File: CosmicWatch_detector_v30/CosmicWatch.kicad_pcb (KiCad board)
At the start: 2 copper layers, 99.9 x 99.9 mm, 81 parts, among them J3 RJ45, P1 CONN_01X04, P10 CONN_02X02, P11 CONN_01X01, P12 CONN_01X01, P13 CONN_01X01, P14 CONN_01X01, P15 CONN_02X04, P16 CONN_01X02, P19 CONN_01X01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

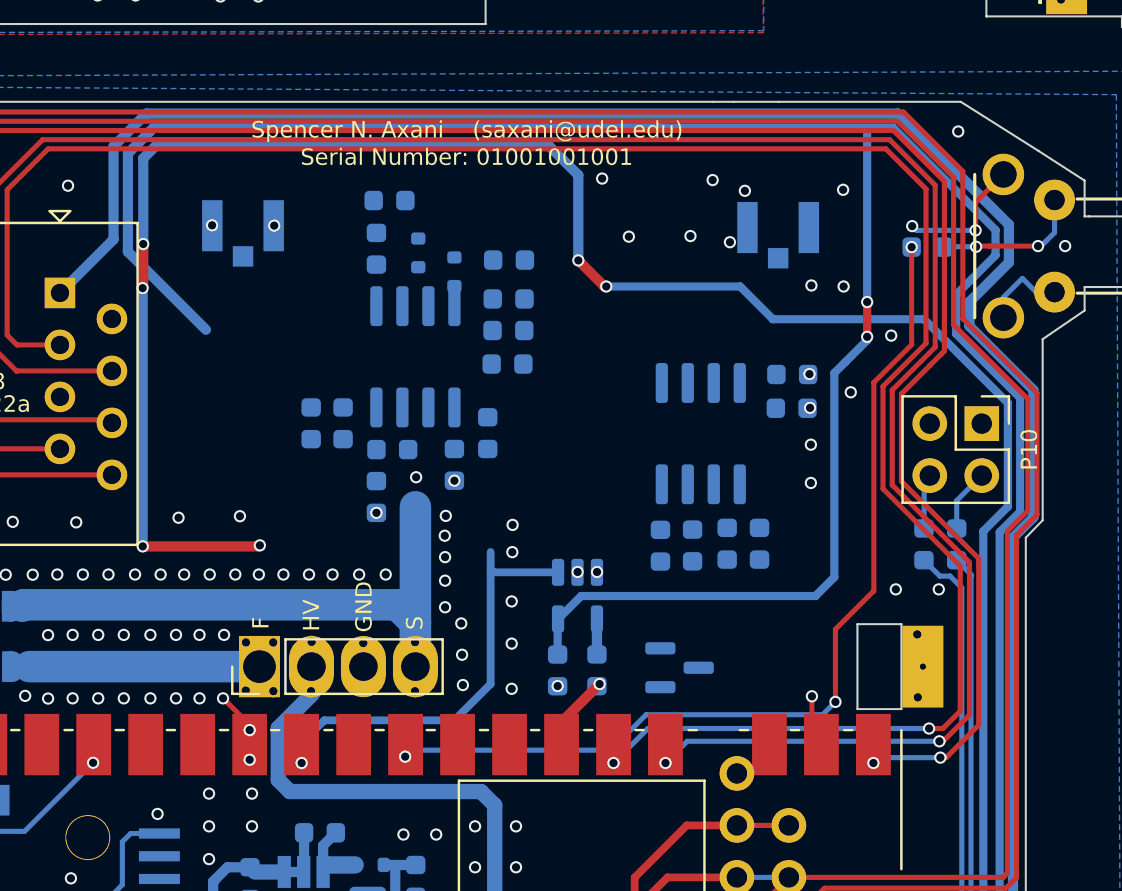
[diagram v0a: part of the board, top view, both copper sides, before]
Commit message: finished peak detector placin and wiring, starting error corrections
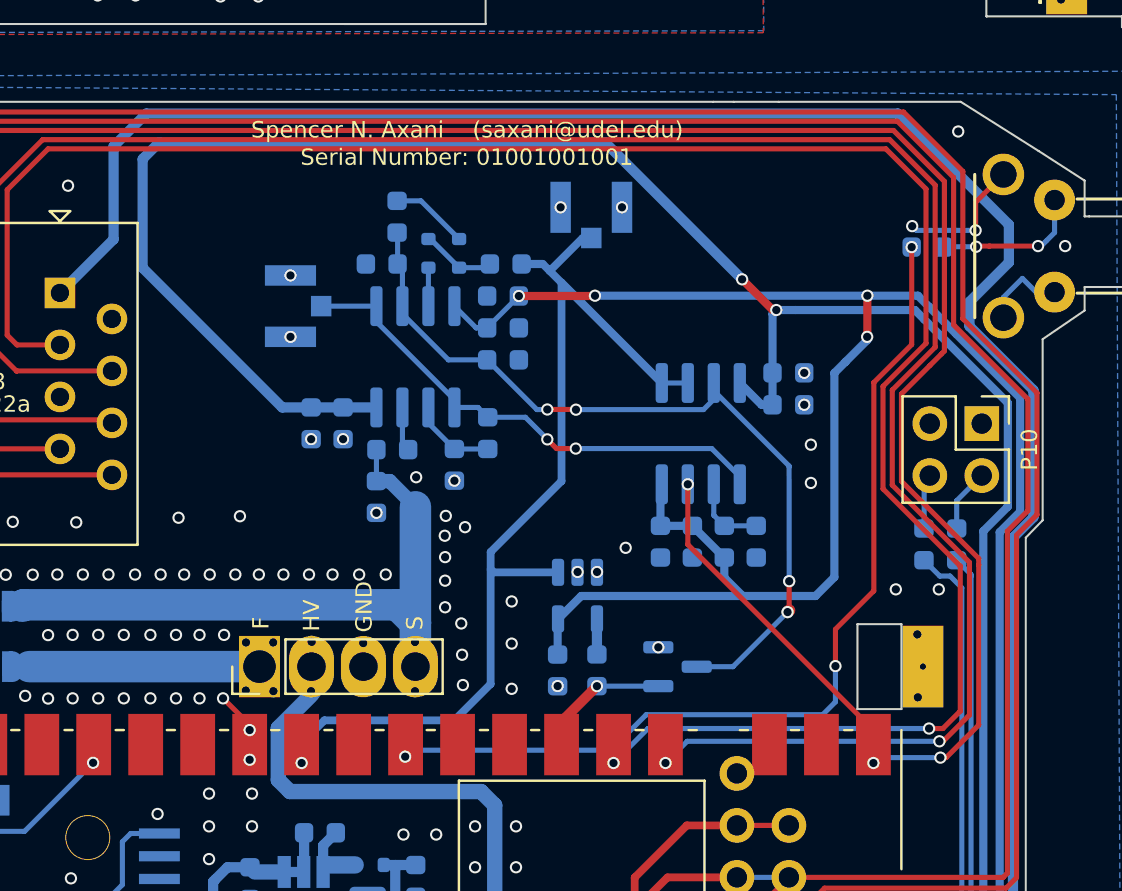
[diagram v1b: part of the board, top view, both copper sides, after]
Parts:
- moved U17 9.18 mm to (176.0, 79.7)
- moved U16 4.56 mm to (161.3, 84.5), turned to 90 degrees
- moved D3 0.93 mm to (169.6, 81.9)
- moved R9 0.87 mm to (166.5, 80.1), turned to 90 degrees
- moved C11 0.79 mm to (165.8, 82.4), turned to 0 degrees
- moved D2 0.50 mm to (168.1, 81.9)
- moved C10 0.31 mm to (171.7, 84.0)
- moved R12 0.30 mm to (171.7, 87.1)
- moved C9 0.29 mm to (171.7, 85.6)
- moved R11 0.25 mm to (171.8, 82.4)
- moved C13 0.23 mm to (185.7, 89.3)
- moved C12 0.21 mm to (185.7, 87.8)
- moved C19 0.20 mm to (179.4, 96.0)
- moved R14 0.19 mm to (184.1, 96.0)
- moved C18 0.19 mm to (181.0, 96.0)
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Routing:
- net Net-(Q1-D): track 0.00 -> 40.7 mm, vias 0 -> 4
- net VCC: track 214.6 -> 179.8 mm, vias 4 -> 6
- net SNG1: track 21.2 -> 49.1 mm, vias 2 -> 1
- net AMP1: track 0.00 -> 24.9 mm, vias 0 -> 2
- net TRG: track 110.4 -> 127.8 mm, vias 2 -> 3
- net Net-(U6--INA): track 0.00 -> 4.19 mm
- net SiPM: track 27.9 -> 31.9 mm
- net Net-(U9--INB): track 0.00 -> 3.80 mm
- net Net-(D3-K): track 0.00 -> 3.80 mm
- net Net-(D2-K): track 0.00 -> 3.66 mm
- net TriggerReset1: track 4.80 -> 7.65 mm
- net TriggerReset2: track 2.80 -> 0.00 mm, vias 1 -> 0
- net Net-(U6-+INA): track 0.00 -> 2.18 mm
- net Net-(D2-A): track 0.00 -> 1.88 mm
- net VEE: track 147.0 -> 146.2 mm, vias 6 -> 2
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
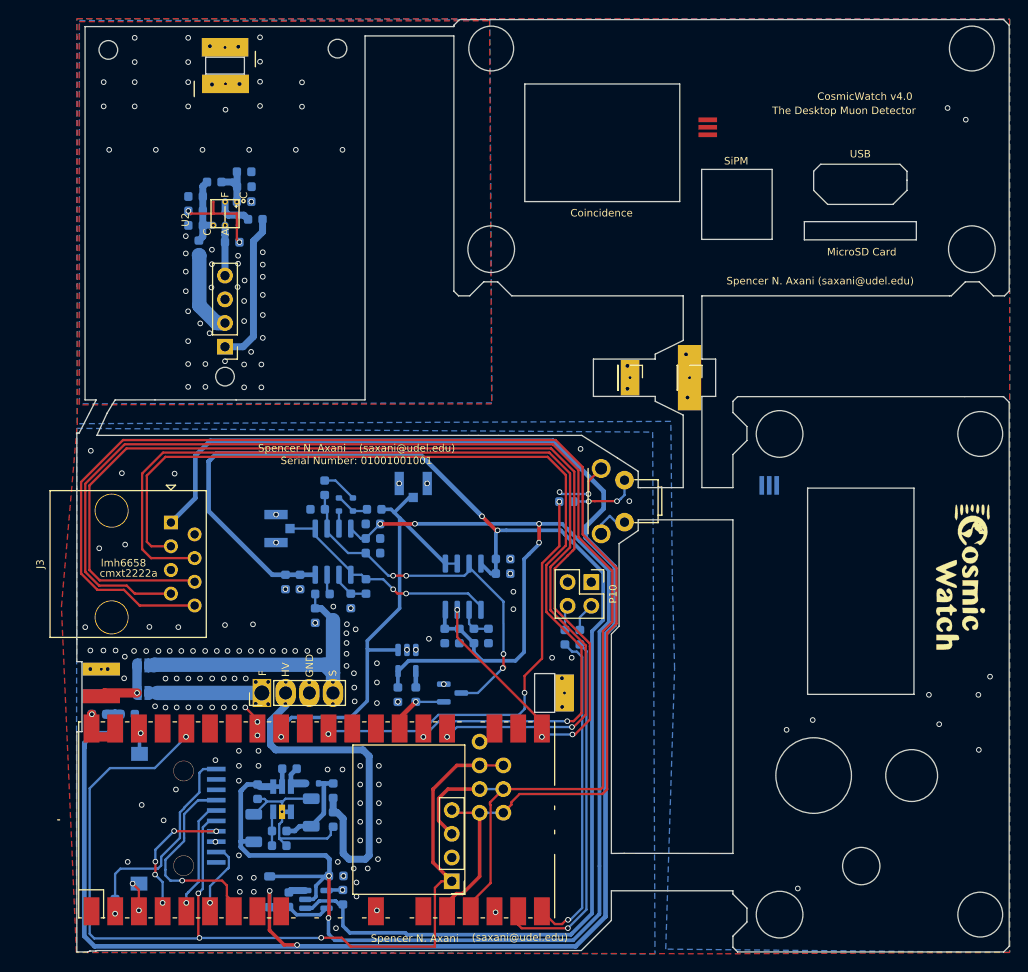
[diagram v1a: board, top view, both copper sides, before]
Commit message: fixed errors, resized SiPM pcb
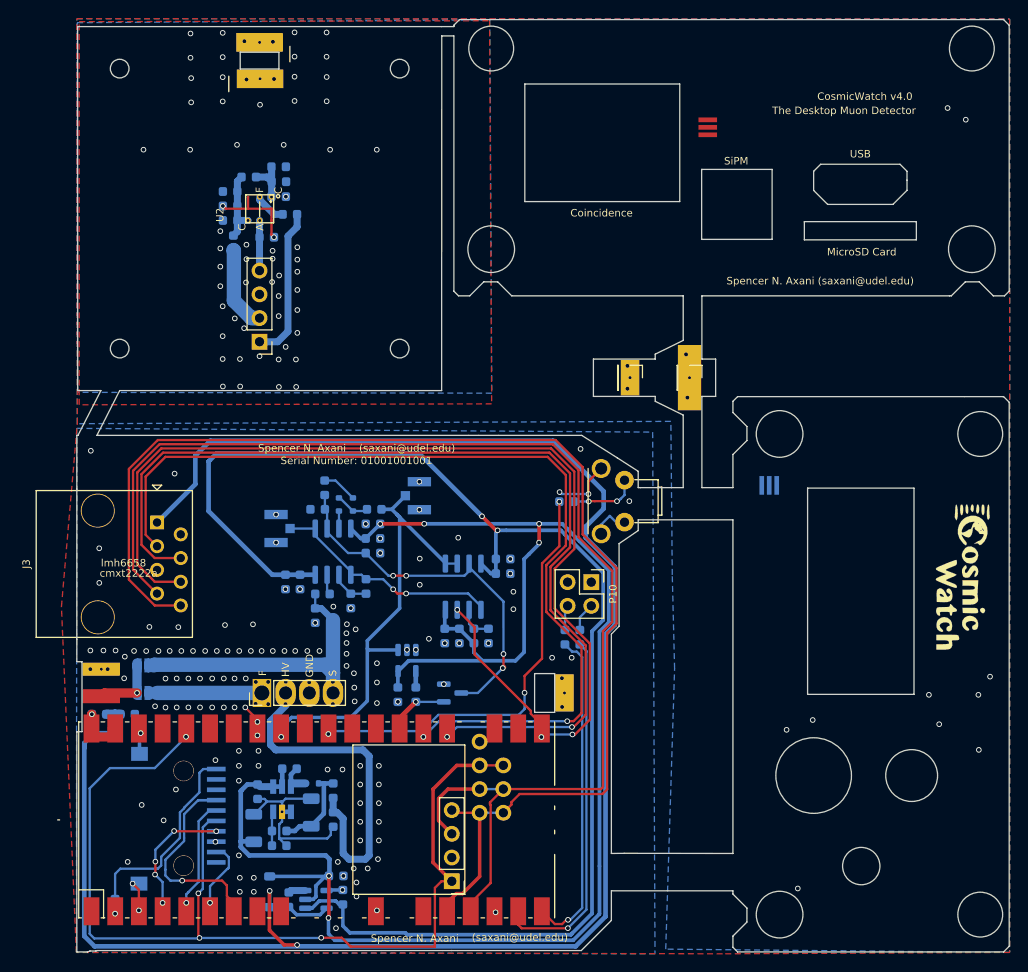
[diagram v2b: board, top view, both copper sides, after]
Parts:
- moved U2 3.75 mm to (159.6, 50.2)
- moved P3 3.74 mm to (159.6, 64.5)
- moved C24 3.74 mm to (162.8, 50.8)
- moved R8 3.74 mm to (160.3, 53.3)
- moved P2 3.74 mm to (159.6, 41.3)
- moved C16 3.74 mm to (161.6, 47.3)
- moved C17 3.74 mm to (161.6, 48.9)
- moved C26 3.74 mm to (156.4, 49.9)
- moved R36 3.74 mm to (158.4, 46.8)
- moved C14 3.74 mm to (156.4, 48.4)
- moved C15 3.74 mm to (161.6, 45.7)
- moved C28 3.74 mm to (156.4, 51.5)
- moved P12 3.74 mm to (159.6, 32.4)
- moved R39 3.74 mm to (156.8, 53.9)
- moved J3 1.49 mm to (148.6, 83.8)
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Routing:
- net TRG: track 127.8 -> 116.5 mm
- net SCL: track 149.7 -> 138.6 mm
- net SDA: track 146.1 -> 135.6 mm
- net CoincidentPin2: track 102.4 -> 100.6 mm
- net CoincidentPin1: track 106.0 -> 104.3 mm
- net VBUS: track 198.3 -> 198.9 mm
- net GNDA: vias 205 -> 212
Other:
- outline, holes or cut-outs redrawn

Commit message: adding some changes
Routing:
- net GNDA: vias 212 -> 180

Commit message: updates
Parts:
- removed C37: 10nF, Capacitor_SMD:C_0603_1608Metric
- removed R7: 1k, Capacitor_SMD:C_0603_1608Metric
- removed U13: TS5A1066, Package_TO_SOT_SMD:SOT-23-5
- P4: moved to B.Cu
- moved P4 12.4 mm to (180.2, 109.9)
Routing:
- net 3.3V: track 107.4 -> 130.2 mm, vias 4 -> 5
- net VCC: track 179.8 -> 168.4 mm
- net SCL: track 138.6 -> 128.1 mm, vias 0 -> 3
- net Net-(U5-GP15): track 38.4 -> 34.9 mm
- net SNG1: track 48.9 -> 45.6 mm
- net SDA: track 135.6 -> 132.4 mm, vias 0 -> 2
- net Net-(U13-IN): track 1.74 -> 0.00 mm
- net unconnected-(U5-ADC0-Pad31): track 1.13 -> 0.00 mm
- net GNDA: track 55.5 -> 54.5 mm, vias 180 -> 171
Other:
- board text removed: "lmh6658"

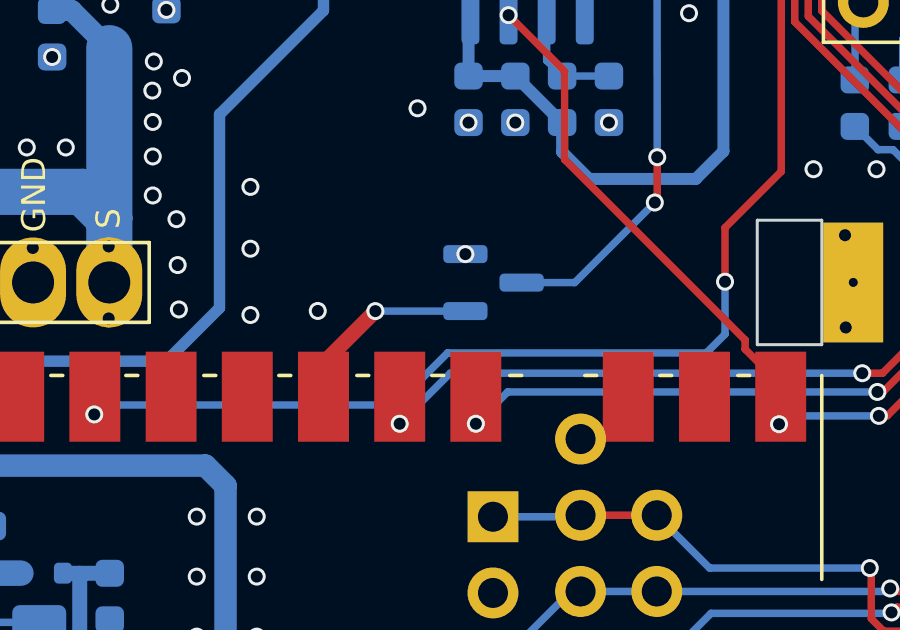
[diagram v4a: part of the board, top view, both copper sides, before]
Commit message: added R5 on trigger reset
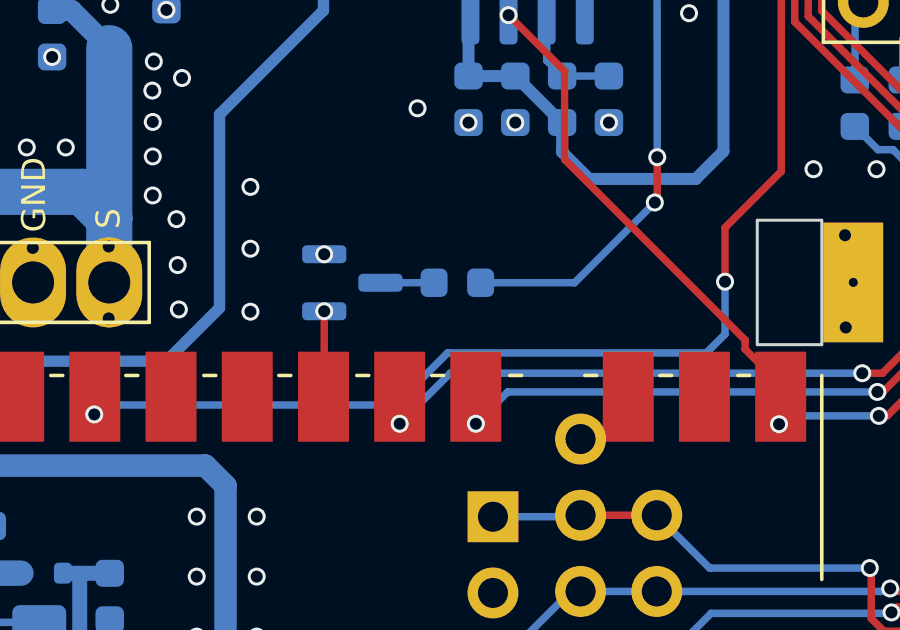
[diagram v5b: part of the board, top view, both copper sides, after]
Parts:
- added R5: 10, Capacitor_SMD:C_0603_1608Metric, B.Cu at (179.0, 102.1)
- moved Q1 4.71 mm to (175.5, 102.1)
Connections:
- C11 pad 2: Net-(Q1-D) -> Net-(U6--INB)
- R12 pad 2: Net-(Q1-D) -> Net-(U6--INB)
- R9 pad 1: Net-(Q1-D) -> Net-(U6--INB)
- U6 pad 6: Net-(Q1-D) -> Net-(U6--INB)
- U9 pad 3: Net-(Q1-D) -> Net-(U6--INB)
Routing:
- net Net-(U6--INB): track 0.00 -> 41.9 mm, vias 0 -> 4
- net Net-(Q1-D): track 40.5 -> 1.79 mm, vias 4 -> 0
- net TriggerReset1: track 7.47 -> 3.76 mm
- net GNDA: vias 171 -> 170
